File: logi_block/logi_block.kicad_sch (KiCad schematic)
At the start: 24 parts, among them J1 Conn_01x02, J2 Conn_02x03_Odd_Even, J3 Conn_02x08_Odd_Even, U1 74HC151, U2 74HC151, U3 74LVC1G157, U4 74LVC1G157, U5 74LVC1G74, U6 74HC164, U7 74HC164

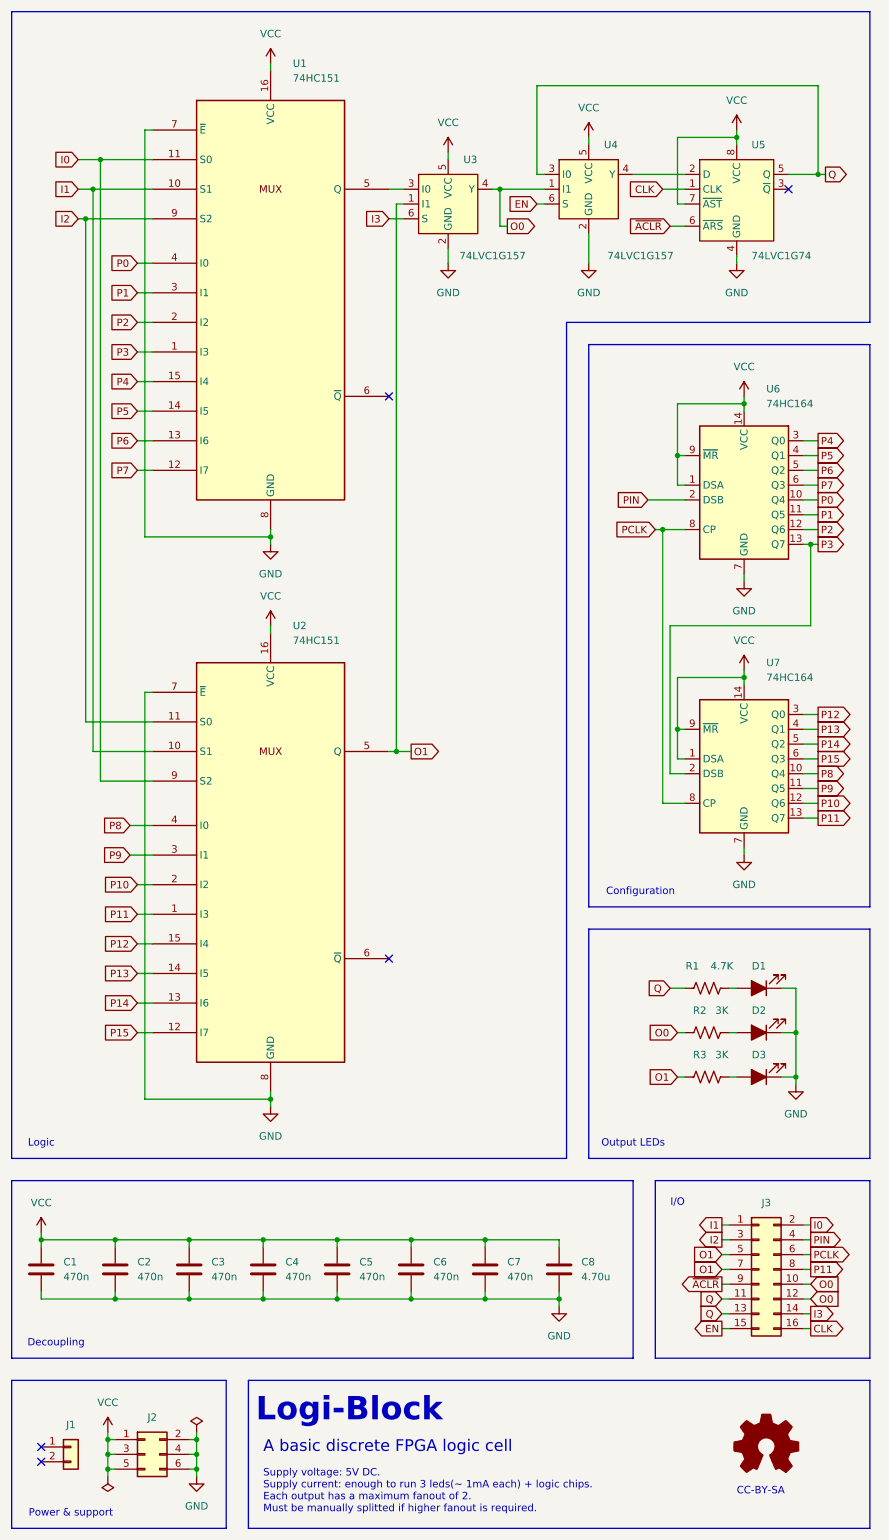
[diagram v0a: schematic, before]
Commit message: Maintenance on schematic Maintenance on PCB (changed serial number for JLCPCB) Added local datasheets Remade pictures Other small refactors...
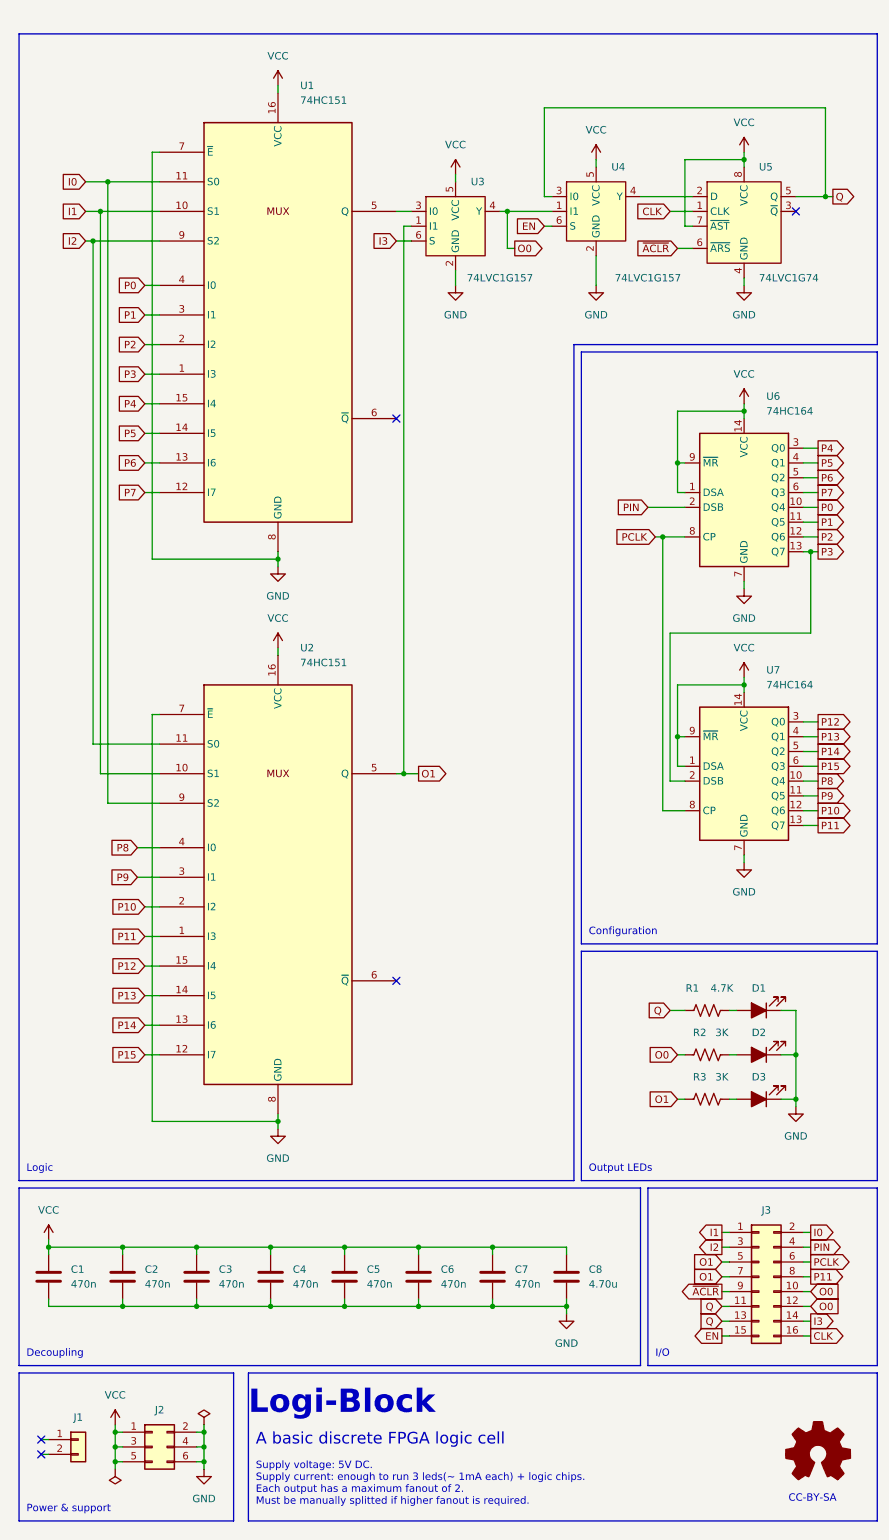
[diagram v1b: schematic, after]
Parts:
- C1, C2, C3, C4, C5, C6, C7, C8, R1, R2, R3: JLCPCB Type Basic -> (none)
- D1, D2, D3, J1, J2, J3, U1, U2, U3, U4, U5, U6, U7: JLCPCB Notes (none) -> extended-part; JLCPCB Type Extended -> (none)
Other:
- moved on the sheet: C1, C2, C3, C4, C5, C6, C7, C8, D1, D2, D3, J1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
